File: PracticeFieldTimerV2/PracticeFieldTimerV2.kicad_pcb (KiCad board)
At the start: 2 copper layers, 106 x 153.7 mm, 34 parts, among them J1 External Controls, J3 Panel, J5 /CAN Enable, J6 RJ45, J7 RJ45, J8 CAN Terminate, U1 ESP32-DevKitC, U2 PCF8574N, U3 20 x 4 LCD, U5 SN65HVD230DR

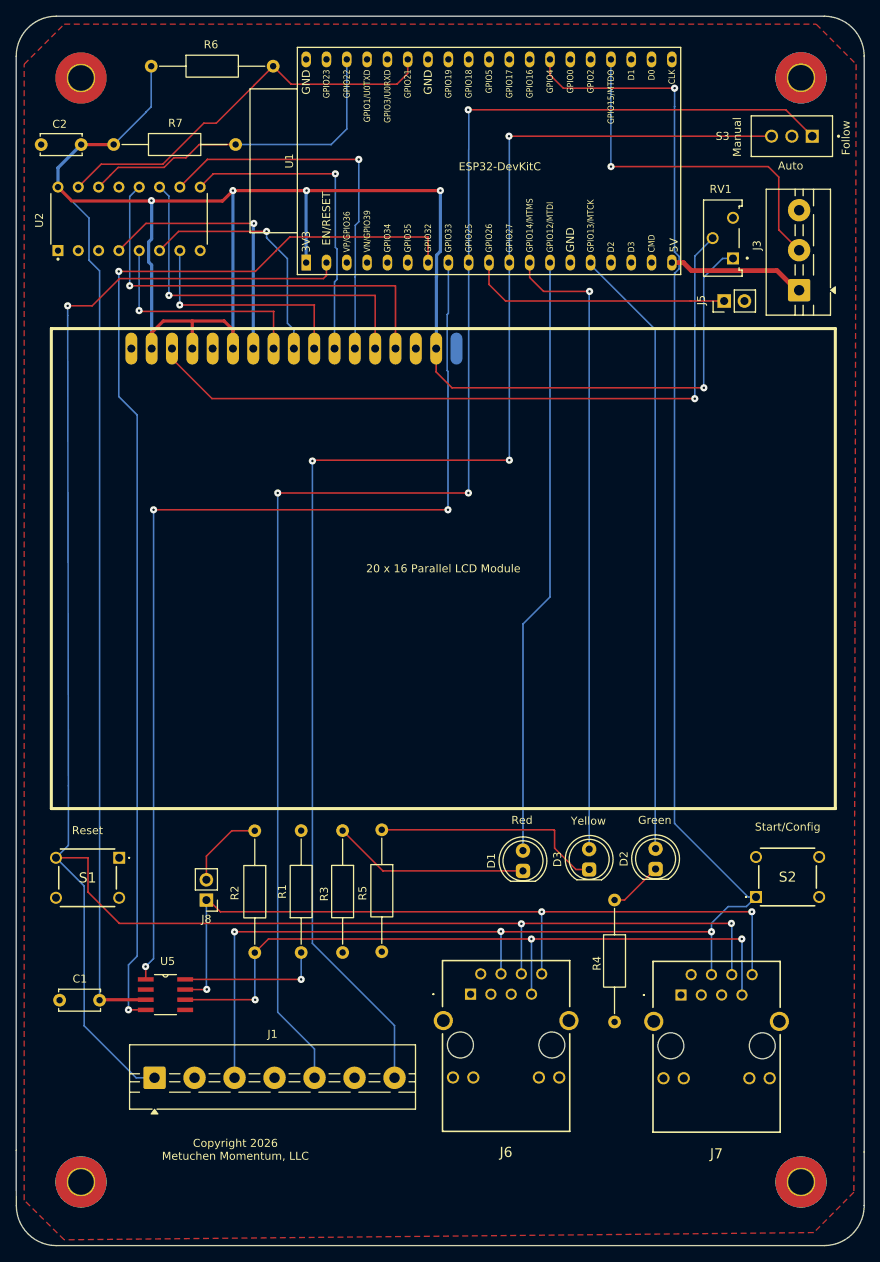
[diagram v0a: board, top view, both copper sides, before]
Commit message: Fix push button connections.
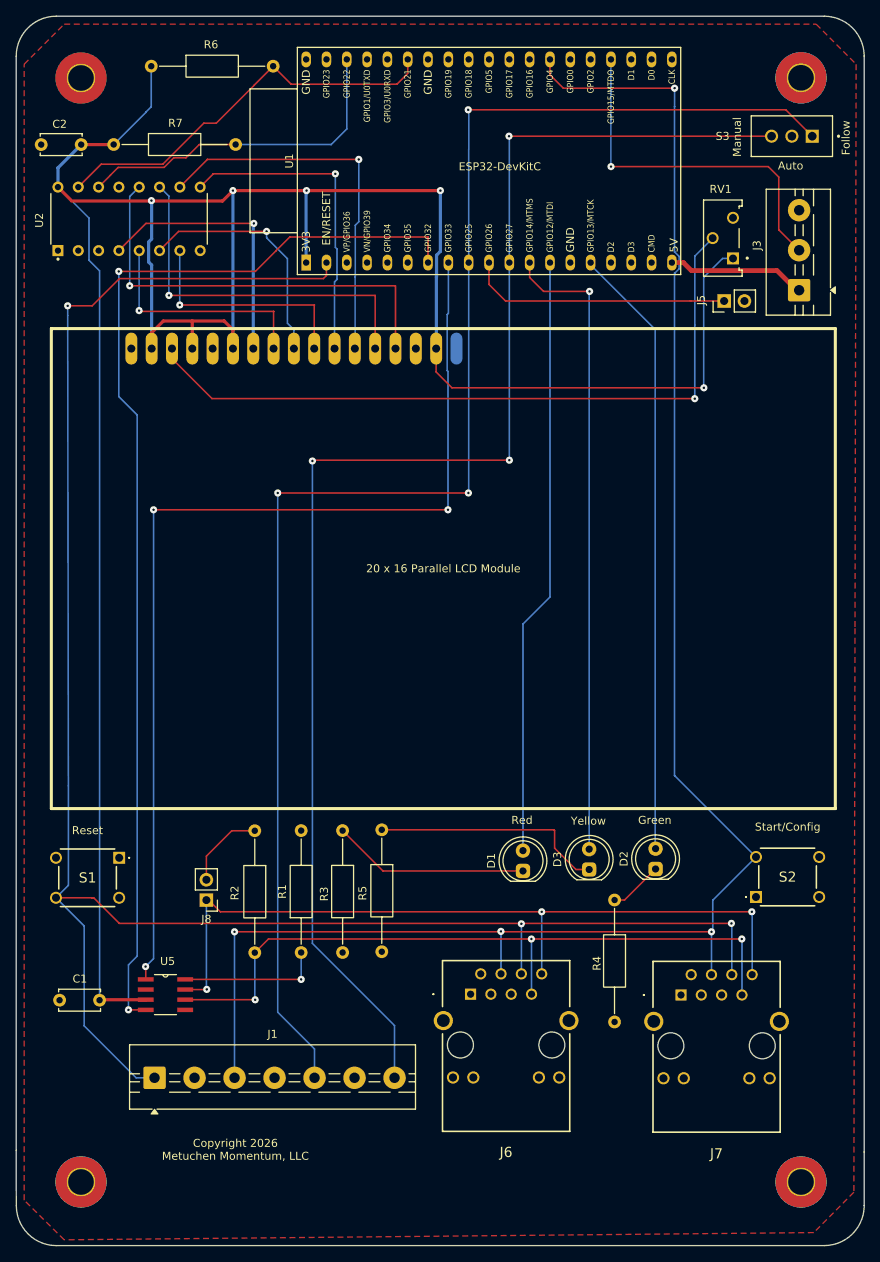
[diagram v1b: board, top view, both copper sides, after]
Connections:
- S1 pad 2: /RST -> unconnected-(S1-COM_2-Pad2)
- S1 pad 4: unconnected-(S1-NO_2-Pad4) -> /RST
- S2 pad 1: /CFG-START -> unconnected-(S2-COM_1-Pad1)
- S2 pad 3: unconnected-(S2-NO_1-Pad3) -> /CFG-START
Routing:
- net /RST: track 242.9 -> 238.3 mm
- net /CFG-START: track 222.6 -> 220.7 mm
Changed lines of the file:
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@@
 	(net 22 "Net-(U5-RS)")
 	(net 23 "unconnected-(S1-NO_1-Pad3)")
-	(net 24 "unconnected-(S1-NO_2-Pad4)")
+	(net 24 "unconnected-(S1-COM_2-Pad2)")
 	(net 25 "unconnected-(S2-NO_2-Pad4)")
-	(net 26 "unconnected-(S2-NO_1-Pad3)")
+	(net 26 "unconnected-(S2-COM_1-Pad1)")
 	(net 27 "unconnected-(U1-VDET_2{slash}GPIO35{slash}ADC1_CH7-Pad6)")
 	(net 28 "unconnected-(U1-GPIO17-Pad28)")
@@
 			(layers "*.Cu" "*.Mask")
 			(remove_unused_layers no)
-			(net 11 "{slash}CFG-START")
+			(net 26 "unconnected-(S2-COM_1-Pad1)")
 			(pinfunction "COM_1")
-			(pintype "passive")
+			(pintype "passive+no_connect")
 		)
 		(pad "2" thru_hole circle
@@
 			(layers "*.Cu" "*.Mask")
 			(remove_unused_layers no)
-			(net 26 "unconnected-(S2-NO_1-Pad3)")
+			(net 11 "{slash}CFG-START")
 			(pinfunction "NO_1")
-			(pintype "passive+no_connect")
+			(pintype "passive")
 		)
 		(pad "4" thru_hole circle
@@
 			(layers "*.Cu" "*.Mask")
 			(remove_unused_layers no)
-			(net 12 "{slash}RST")
+			(net 24 "unconnected-(S1-COM_2-Pad2)")
 			(pinfunction "COM_2")
-			(pintype "passive")
+			(pintype "passive+no_connect")
 		)
 		(pad "3" thru_hole circle
@@
 			(layers "*.Cu" "*.Mask")
 			(remove_unused_layers no)
-			(net 24 "unconnected-(S1-NO_2-Pad4)")
+			(net 12 "{slash}RST")
 			(pinfunction "NO_2")
-			(pintype "passive+no_connect")
+			(pintype "passive")
 		)
 		(embedded_fonts no)
@@
 		(effects
 			(font
-				(size 1 1)
+				(size 1.5 1.5)
 				(thickness 0.15)
 			)
@@
 		(effects
 			(font
-				(size 1 1)
+				(size 1.5 1.5)
 				(thickness 0.15)
 			)
@@
 	)
 	(segment
-		(start 122.291405 34.3)
-		(end 122.291405 52.496963)
+		(start 122.335294 52.496963)
+		(end 122.863088 53.024757)
 		(width 0.2)
 		(layer "B.Cu")
@@
 	)
 	(segment
-		(start 132.472088 133.097963)
-		(end 131.272088 134.297963)
+		(start 122.291405 34.3)
+		(end 122.291405 52.496963)
 		(width 0.2)
 		(layer "B.Cu")
@@
 	)
 	(segment
-		(start 100.591405 137.4)
-		(end 100.606405 137.415)
+		(start 122.291405 55.098963)
+		(end 122.291405 117.91728)
 		(width 0.2)
 		(layer "B.Cu")
@@
 	)
 	(segment
-		(start 122.863088 53.024757)
-		(end 122.863088 54.571169)
+		(start 122.3 34.291405)
+		(end 122.291405 34.3)
 		(width 0.2)
 		(layer "B.Cu")
@@
 	)
 	(segment
-		(start 126.911405 142.807963)
-		(end 126.911405 137.48)
+		(start 132.472088 128.097963)
+		(end 127.07 133.500051)
 		(width 0.2)
 		(layer "B.Cu")
@@
 	)
 	(segment
-		(start 122.3 34.291405)
-		(end 122.291405 34.3)
+		(start 122.863088 53.024757)
+		(end 122.863088 54.571169)
 		(width 0.2)
 		(layer "B.Cu")
@@
 	)
 	(segment
-		(start 126.911405 136.38)
-		(end 126.911405 137.447963)
+		(start 100.591405 137.4)
+		(end 100.606405 137.415)
 		(width 0.2)
 		(layer "B.Cu")
@@
 	)
 	(segment
-		(start 128.993442 134.297963)
-		(end 126.911405 136.38)
+		(start 122.863088 54.571169)
+		(end 122.335294 55.098963)
 		(width 0.2)
 		(layer "B.Cu")
@@
 	)
 	(segment
-		(start 122.335294 55.098963)
-		(end 122.291405 55.098963)
+		(start 122.291405 117.91728)
+		(end 122.291405 117.9)
 		(width 0.2)
 		(layer "B.Cu")
@@
 	)
 	(segment
-		(start 122.291405 123.9)
-		(end 131.489368 133.097963)
+		(start 126.911405 142.807963)
+		(end 126.911405 137.48)
 		(width 0.2)
 		(layer "B.Cu")
@@
 	)
 	(segment
-		(start 122.3 32)
-		(end 122.3 34.291405)
+		(start 127.07 133.500051)
+		(end 127.07 137.289368)
 		(width 0.2)
 		(layer "B.Cu")
@@
 	)
 	(segment
-		(start 122.291405 55.098963)
-		(end 122.291405 123.9)
+		(start 127.07 137.289368)
+		(end 126.911405 137.447963)
 		(width 0.2)
 		(layer "B.Cu")
@@
 	)
 	(segment
-		(start 67.291405 155.697963)
-		(end 67.291405 137.447963)
+		(start 122.335294 55.098963)
+		(end 122.291405 55.098963)
 		(width 0.2)
 		(layer "B.Cu")
@@
 	)
 	(segment
-		(start 122.863088 54.571169)
-		(end 122.335294 55.098963)
+		(start 67.291405 155.697963)
+		(end 67.291405 137.447963)
 		(width 0.2)
 		(layer "B.Cu")
@@
 	)
 	(segment
-		(start 122.335294 52.496963)
-		(end 122.863088 53.024757)
+		(start 122.3 32)
+		(end 122.3 34.291405)
 		(width 0.2)
 		(layer "B.Cu")
@@
 	)
 	(segment
-		(start 131.272088 134.297963)
-		(end 128.993442 134.297963)
+		(start 132.472088 128.097963)
+		(end 122.291405 117.91728)
 		(width 0.2)
 		(layer "B.Cu")
@@
 	)
 	(segment
-		(start 131.489368 133.097963)
-		(end 132.472088 133.097963)
+		(start 67.022088 155.697963)
+		(end 68.022088 154.697963)
 		(width 0.2)
 		(layer "B.Cu")
@@
 	)
 	(segment
-		(start 67.022088 155.697963)
-		(end 68.022088 154.697963)
-		(width 0.2)
-		(layer "B.Cu")
-		(net 11)
-	)
-	(segment
 		(start 100.606405 137.415)
 		(end 100.606405 142.707963)
@@
 	)
 	(segment
+		(start 49.695703 133.204297)
+		(end 52.891405 136.4)
+		(width 0.2)
+		(layer "F.Cu")
+		(net 12)
+	)
+	(segment
 		(start 49.5 59.2)
 		(end 52.9 55.8)
@@
 	)
 	(segment
-		(start 48.972088 128.197963)
-		(end 48.972088 132.480683)
+		(start 49.472037 133.197963)
+		(end 49.478371 133.204297)
 		(width 0.2)
 		(layer "F.Cu")
@@
 	)
 	(segment
-		(start 78.4 55.8)
-		(end 78.782088 55.417912)
+		(start 49.478371 133.204297)
+		(end 49.695703 133.204297)
 		(width 0.2)
 		(layer "F.Cu")
@@
 	)
 	(segment
-		(start 52.9 55.8)
-		(end 78.4 55.8)
+		(start 44.972088 133.197963)
+		(end 49.472037 133.197963)
 		(width 0.2)
 		(layer "F.Cu")
@@
 	)
 	(segment
-		(start 48.972088 132.480683)
-		(end 52.891405 136.4)
+		(start 78.4 55.8)
+		(end 78.782088 55.417912)
 		(width 0.2)
 		(layer "F.Cu")
@@
 	)
 	(segment
-		(start 78.782088 53.457963)
-		(end 78.782088 53.797963)
+		(start 52.9 55.8)
+		(end 78.4 55.8)
 		(width 0.2)
 		(layer "F.Cu")
@@
 	)
 	(segment
-		(start 44.972088 128.197963)
-		(end 48.972088 128.197963)
+		(start 78.782088 53.457963)
+		(end 78.782088 53.797963)
 		(width 0.2)
 		(layer "F.Cu")
@@
 	)
 	(segment
-		(start 129.451405 136.447963)
-		(end 129.401405 136.397963)
+		(start 46.43675 59.201741)
+		(end 46.43675 60.4)
 		(width 0.2)
 		(layer "B.Cu")
@@
 	(segment
 		(start 46.522088 119.197963)
-		(end 46.522088 126.647963)
+		(end 46.522088 131.647963)
 		(width 0.2)
 		(layer "B.Cu")
@@
 	)
 	(segment
-		(start 46.43675 60.4)
-		(end 46.43675 59.201741)
+		(start 129.451405 136.447963)
+		(end 129.401405 136.397963)
 		(width 0.2)
 		(layer "B.Cu")
@@
 	)
 	(segment
-		(start 48.491405 149.2)
-		(end 48.491405 131.71728)
+		(start 46.522088 131.647963)
+		(end 44.972088 133.197963)
 		(width 0.2)
 		(layer "B.Cu")
@@
 	)
 	(segment
-		(start 46.522088 126.647963)
-		(end 44.972088 128.197963)
+		(start 46.43675 60.4)
+		(end 46.522088 119.197963)
 		(width 0.2)
 		(layer "B.Cu")
@@
 	)
 	(segment
-		(start 129.451405 142.807963)
-		(end 129.451405 136.447963)
+		(start 48.464125 136.69)
+		(end 48.491405 136.69)
 		(width 0.2)
 		(layer "B.Cu")
@@
 	)
 	(segment
-		(start 57.291405 155.697963)
-		(end 54.989368 155.697963)
+		(start 48.491405 149.2)
+		(end 48.491405 136.69)
 		(width 0.2)
 		(layer "B.Cu")
@@
 	)
 	(segment
-		(start 103.146405 142.707963)
-		(end 103.146405 136.447963)
+		(start 129.451405 142.807963)
+		(end 129.451405 136.447963)
 		(width 0.2)
 		(layer "B.Cu")
@@
 	)
 	(segment
-		(start 48.491405 149.2)
+		(start 57.291405 155.697963)
 		(end 54.989368 155.697963)
 		(width 0.2)
@@
 	)
 	(segment
-		(start 46.43675 60.4)
-		(end 46.522088 119.197963)
+		(start 46.435009 59.2)
+		(end 46.43675 59.201741)
 		(width 0.2)
 		(layer "B.Cu")
@@
 	)
 	(segment
-		(start 46.43675 59.201741)
-		(end 46.435009 59.2)
+		(start 103.146405 142.707963)
+		(end 103.146405 136.447963)
+		(width 0.2)
+		(layer "B.Cu")
+		(net 12)
+	)
+	(segment
+		(start 48.491405 149.2)
+		(end 54.989368 155.697963)
 		(width 0.2)
 		(layer "B.Cu")
@@
 	)
 	(segment
-		(start 48.491405 131.71728)
-		(end 44.972088 128.197963)
+		(start 44.972088 133.197963)
+		(end 48.464125 136.69)
 		(width 0.2)
 		(layer "B.Cu")

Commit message: Add DS3231
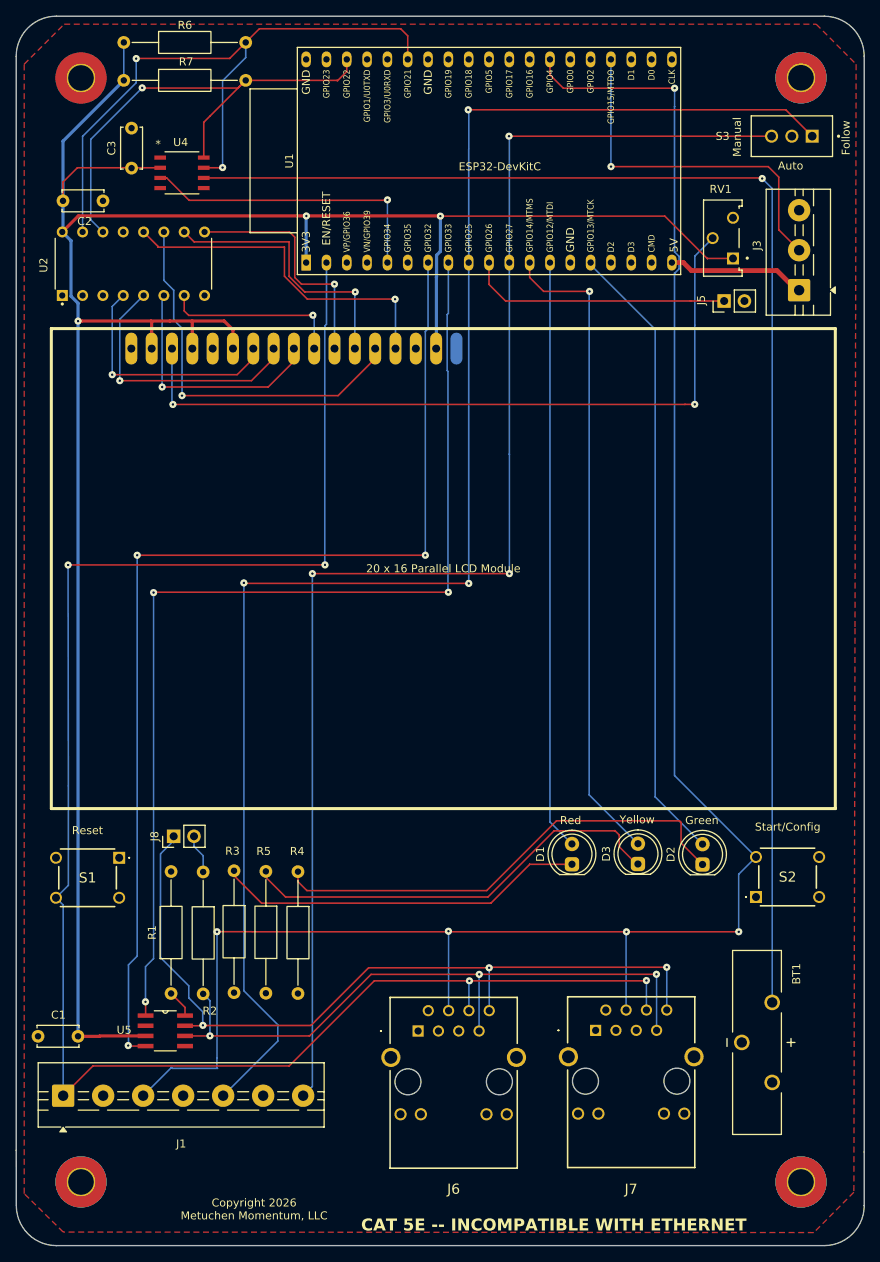
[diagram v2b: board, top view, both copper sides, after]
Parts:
- added BT1: 1074, Misc:BAT_1074, F.Cu at (132.6, 151.3)
- added C3: 100n, Capacitor_THT:C_Disc_D5.0mm_W2.5mm_P5.00mm, F.Cu at (54.4, 42.0)
- added U4: DS3231MZ_TRL, Misc:21-0041B_8_MXM, F.Cu at (60.7, 42.6)
- moved R4 39.7 mm to (75.2, 129.9)
- moved R1 17.0 mm to (59.4, 145.2)
- moved R5 15.4 mm to (71.2, 129.9)
- moved R3 14.5 mm to (67.2, 129.8)
- moved J1 11.6 mm to (45.9, 157.9)
- moved J7 11.6 mm to (112.4, 149.8)
- moved J8 8.96 mm to (59.7, 125.5), turned to 90 degrees
- moved R2 8.26 mm to (63.4, 130.0)
- moved R7 8.12 mm to (53.5, 31.0)
- moved J6 8.01 mm to (90.2, 149.8)
- moved C2 7.39 mm to (45.9, 46.1), turned to 0 degrees
- moved D1 6.18 mm to (109.5, 129.0)
- moved D3 6.14 mm to (117.7, 129.0)
- moved D2 5.89 mm to (125.8, 129.0)
- moved U2 5.64 mm to (54.6, 53.9)
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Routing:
- net Net-(U4-VBAT): track 0.00 -> 173.3 mm, vias 0 -> 1
- net Net-(D2-K): track 6.74 -> 59.7 mm
- net SQW: track 0.00 -> 37.4 mm, vias 0 -> 1
- net I2C SDA: track 50.7 -> 82.4 mm, vias 0 -> 2
- net +3.3V: track 322.2 -> 293.7 mm, vias 5 -> 3
- net Net-(D3-K): track 29.3 -> 54.5 mm
- net Net-(D1-K): track 24.6 -> 46.5 mm
- net /CFG-START: track 220.7 -> 242.1 mm, vias 4 -> 5
- net I2C SCL: track 42.8 -> 61.1 mm, vias 0 -> 1
- net Net-(U5-RS): track 17.9 -> 3.49 mm, vias 1 -> 0
- net /RST: track 238.3 -> 224.6 mm, vias 3 -> 4
- net Net-(U2-P5): track 46.4 -> 34.1 mm
- net Net-(U2-P7): track 53.9 -> 43.3 mm
- net Net-(U2-P4): track 39.8 -> 30.0 mm
- net /Follow: track 191.0 -> 200.4 mm
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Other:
- board text added: "CAT 5E -- INCOMPATIBLE WITH ETHERNET"

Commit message: Morar blinkinlights: connect the LEDs on the RJ45 jacks to ESP32 pins. Can have too many blinkers!
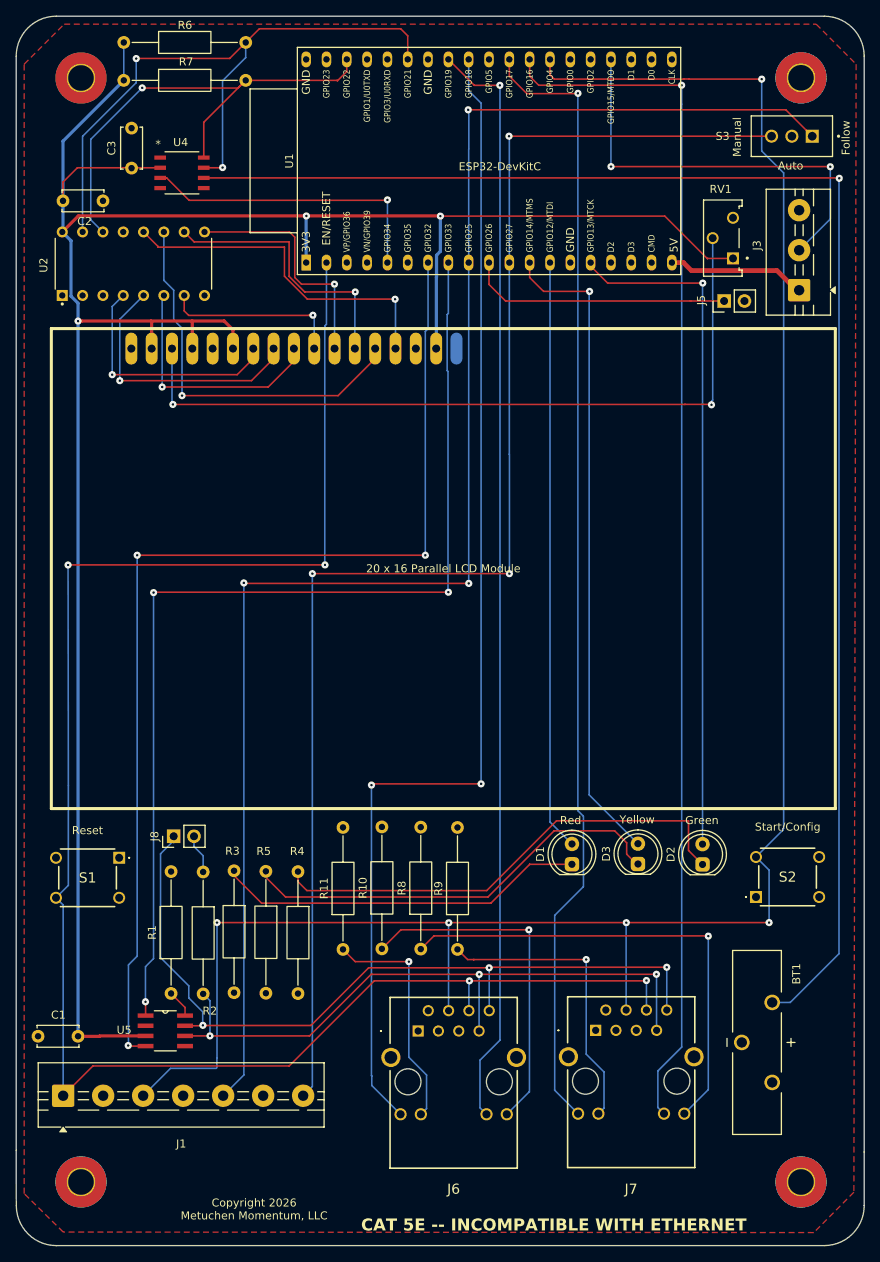
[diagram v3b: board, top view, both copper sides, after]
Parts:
- added R10: 510, Resistor_THT:R_Axial_DIN0207_L6.3mm_D2.5mm_P15.24mm_Horizontal, F.Cu at (85.7, 139.6)
- added R11: 510, Resistor_THT:R_Axial_DIN0207_L6.3mm_D2.5mm_P15.24mm_Horizontal, F.Cu at (80.8, 139.7)
- added R8: 510, Resistor_THT:R_Axial_DIN0207_L6.3mm_D2.5mm_P15.24mm_Horizontal, F.Cu at (90.6, 139.6)
- added R9: 510, Resistor_THT:R_Axial_DIN0207_L6.3mm_D2.5mm_P15.24mm_Horizontal, F.Cu at (95.2, 139.7)
- J6: value RJ45 -> RJ45-B
- J7: value RJ45 -> RJ45-A
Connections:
- J6 pad 10: unconnected-(J6-K_YELLOW-Pad10) -> Net-(J6-K_YELLOW)
- J6 pad 11: unconnected-(J6-A_GREEN-Pad11) -> /RJ45-B-Green
- J6 pad 12: unconnected-(J6-K_GREEN-Pad12) -> Net-(J6-K_GREEN)
- J6 pad 13: unconnected-(J6-MH1-Pad13) -> GND
- J6 pad 14: unconnected-(J6-MH2-Pad14) -> GND
- J6 pad 9: unconnected-(J6-A_YELLOW-Pad9) -> /RJ45-B-Yellow
- J7 pad 10: unconnected-(J7-K_YELLOW-Pad10) -> Net-(J7-K_YELLOW)
- J7 pad 11: unconnected-(J7-A_GREEN-Pad11) -> /RJ45-A-Green
- J7 pad 12: unconnected-(J7-K_GREEN-Pad12) -> Net-(J7-K_GREEN)
- J7 pad 13: unconnected-(J7-MH1-Pad13) -> GND
- J7 pad 14: unconnected-(J7-MH2-Pad14) -> GND
- J7 pad 9: unconnected-(J7-A_YELLOW-Pad9) -> /RJ45-A-Yellow
- U1 pad 27: unconnected-(U1-GPIO16-Pad27) -> /RJ45-A-Green
- U1 pad 28: unconnected-(U1-GPIO17-Pad28) -> /RJ45-A-Yellow
- U1 pad 30: unconnected-(U1-GPIO18-Pad30) -> /RJ45-B-Yellow
- U1 pad 31: unconnected-(U1-GPIO19-Pad31) -> /RJ45-B-Green
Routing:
- net /RJ45-A-Green: track 0.00 -> 151.7 mm, vias 0 -> 1
- net /RJ45-B-Yellow: track 0.00 -> 147.6 mm, vias 0 -> 2
- net /RJ45-A-Yellow: track 0.00 -> 142.1 mm, vias 0 -> 1
- net /RJ45-B-Green: track 0.00 -> 137.8 mm, vias 0 -> 1
- net Net-(J7-K_GREEN): track 0.00 -> 60.1 mm, vias 0 -> 1
- net Net-(J6-K_GREEN): track 0.00 -> 43.6 mm, vias 0 -> 1
- net Net-(J7-K_YELLOW): track 0.00 -> 37.1 mm, vias 0 -> 1
- net Net-(J6-K_YELLOW): track 0.00 -> 29.2 mm, vias 0 -> 1
- net /CFG-START: track 242.1 -> 257.0 mm
- net Net-(U4-VBAT): track 173.3 -> 187.3 mm
- net Panel DOUT: track 45.1 -> 52.9 mm, vias 1 -> 2
- net Net-(D2-A): track 78.0 -> 85.5 mm, vias 0 -> 1
- net /Follow: track 200.4 -> 196.8 mm
- net Net-(U3-V0): track 94.0 -> 95.3 mm
- net Net-(D2-K): track 59.7 -> 60.4 mm
